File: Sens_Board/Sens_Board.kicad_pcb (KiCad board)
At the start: 4 copper layers, 87 x 84 mm, 170 parts, among them J1 Conn_01x09_Pin, J2 Conn_01x09_Pin, U1 74HC595, U10 74HC165, U11 74HC165, U12 74HC165, U13 74HC165, U14 74HC165, U15 74HC165, U2 74HC595, U3 74HC595, U4 74HC165, U5 74HC165, U6 74HC165, U7 74HC165, U8 74HC165, U9 74HC165

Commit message: fixes and optmierung
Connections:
- J3 pad A1: /RJ45/SchieberegisterInput/D7 -> /RJ45/SchieberegisterInput/D4
- J3 pad A2: /RJ45/SchieberegisterInput/D6 -> /RJ45/SchieberegisterInput/D5
- J3 pad A3: /RJ45/SchieberegisterInput/D5 -> /RJ45/SchieberegisterInput/D6
- J3 pad A4: /RJ45/SchieberegisterInput/D4 -> /RJ45/SchieberegisterInput/D7
- J3 pad A5: /RJ45/SchieberegisterInput/D3 -> /RJ45/SchieberegisterInput/D0
- J3 pad A6: /RJ45/SchieberegisterInput/D2 -> /RJ45/SchieberegisterInput/D1
- J3 pad A7: /RJ45/SchieberegisterInput/D1 -> /RJ45/SchieberegisterInput/D2
- J3 pad A8: /RJ45/SchieberegisterInput/D0 -> /RJ45/SchieberegisterInput/D3
- J3 pad B1: /RJ45/SchieberegisterInput1/D7 -> /RJ45/SchieberegisterInput1/D4
- J3 pad B2: /RJ45/SchieberegisterInput1/D6 -> /RJ45/SchieberegisterInput1/D5
- J3 pad B3: /RJ45/SchieberegisterInput1/D5 -> /RJ45/SchieberegisterInput1/D6
- J3 pad B4: /RJ45/SchieberegisterInput1/D4 -> /RJ45/SchieberegisterInput1/D7
- J3 pad B5: /RJ45/SchieberegisterInput1/D3 -> /RJ45/SchieberegisterInput1/D0
- J3 pad B6: /RJ45/SchieberegisterInput1/D2 -> /RJ45/SchieberegisterInput1/D1
- J3 pad B7: /RJ45/SchieberegisterInput1/D1 -> /RJ45/SchieberegisterInput1/D2
- J3 pad B8: /RJ45/SchieberegisterInput1/D0 -> /RJ45/SchieberegisterInput1/D3
- J3 pad C1: /RJ45/SchieberegisterInput2/D7 -> /RJ45/SchieberegisterInput2/D4
- J3 pad C2: /RJ45/SchieberegisterInput2/D6 -> /RJ45/SchieberegisterInput2/D5
- J3 pad C3: /RJ45/SchieberegisterInput2/D5 -> /RJ45/SchieberegisterInput2/D6
- J3 pad C4: /RJ45/SchieberegisterInput2/D4 -> /RJ45/SchieberegisterInput2/D7
- J3 pad C5: /RJ45/SchieberegisterInput2/D3 -> /RJ45/SchieberegisterInput2/D0
- J3 pad C6: /RJ45/SchieberegisterInput2/D2 -> /RJ45/SchieberegisterInput2/D1
- J3 pad C7: /RJ45/SchieberegisterInput2/D1 -> /RJ45/SchieberegisterInput2/D2
- J3 pad C8: /RJ45/SchieberegisterInput2/D0 -> /RJ45/SchieberegisterInput2/D3
- J3 pad D1: /RJ45/SchieberegisterInput3/D7 -> /RJ45/SchieberegisterInput3/D4
- J3 pad D2: /RJ45/SchieberegisterInput3/D6 -> /RJ45/SchieberegisterInput3/D5
- J3 pad D3: /RJ45/SchieberegisterInput3/D5 -> /RJ45/SchieberegisterInput3/D6
- J3 pad D4: /RJ45/SchieberegisterInput3/D4 -> /RJ45/SchieberegisterInput3/D7
- J3 pad D5: /RJ45/SchieberegisterInput3/D3 -> /RJ45/SchieberegisterInput3/D0
- J3 pad D6: /RJ45/SchieberegisterInput3/D2 -> /RJ45/SchieberegisterInput3/D1
- J3 pad D7: /RJ45/SchieberegisterInput3/D1 -> /RJ45/SchieberegisterInput3/D2
- J3 pad D8: /RJ45/SchieberegisterInput3/D0 -> /RJ45/SchieberegisterInput3/D3
- J3 pad E1: /RJ45/SchieberegisterInput4/D7 -> /RJ45/SchieberegisterInput4/D4
- J3 pad E2: /RJ45/SchieberegisterInput4/D6 -> /RJ45/SchieberegisterInput4/D5
- J3 pad E3: /RJ45/SchieberegisterInput4/D5 -> /RJ45/SchieberegisterInput4/D6
- J3 pad E4: /RJ45/SchieberegisterInput4/D4 -> /RJ45/SchieberegisterInput4/D7
- J3 pad E5: /RJ45/SchieberegisterInput4/D3 -> /RJ45/SchieberegisterInput4/D0
- J3 pad E6: /RJ45/SchieberegisterInput4/D2 -> /RJ45/SchieberegisterInput4/D1
- J3 pad E7: /RJ45/SchieberegisterInput4/D1 -> /RJ45/SchieberegisterInput4/D2
- J3 pad E8: /RJ45/SchieberegisterInput4/D0 -> /RJ45/SchieberegisterInput4/D3
- J3 pad F1: /RJ45/SchieberegisterInput5/D7 -> /RJ45/SchieberegisterInput5/D4
- J3 pad F11: (no net) -> GND
- J3 pad F12: GND -> /OutputShift1/Out3
- J3 pad F2: /RJ45/SchieberegisterInput5/D6 -> /RJ45/SchieberegisterInput5/D5
- J3 pad F3: /RJ45/SchieberegisterInput5/D5 -> /RJ45/SchieberegisterInput5/D6
- J3 pad F4: /RJ45/SchieberegisterInput5/D4 -> /RJ45/SchieberegisterInput5/D7
- J3 pad F5: /RJ45/SchieberegisterInput5/D3 -> /RJ45/SchieberegisterInput5/D0
- J3 pad F6: /RJ45/SchieberegisterInput5/D2 -> /RJ45/SchieberegisterInput5/D1
- J3 pad F7: /RJ45/SchieberegisterInput5/D1 -> /RJ45/SchieberegisterInput5/D2
- J3 pad F8: /RJ45/SchieberegisterInput5/D0 -> /RJ45/SchieberegisterInput5/D3
- J3 pad G1: /RJ45/SchieberegisterInput6/D7 -> /RJ45/SchieberegisterInput6/D4
- J3 pad G2: /RJ45/SchieberegisterInput6/D6 -> /RJ45/SchieberegisterInput6/D5
- J3 pad G3: /RJ45/SchieberegisterInput6/D5 -> /RJ45/SchieberegisterInput6/D6
- J3 pad G4: /RJ45/SchieberegisterInput6/D4 -> /RJ45/SchieberegisterInput6/D7
- J3 pad G5: /RJ45/SchieberegisterInput6/D3 -> /RJ45/SchieberegisterInput6/D0
- J3 pad G6: /RJ45/SchieberegisterInput6/D2 -> /RJ45/SchieberegisterInput6/D1
- J3 pad G7: /RJ45/SchieberegisterInput6/D1 -> /RJ45/SchieberegisterInput6/D2
- J3 pad G8: /RJ45/SchieberegisterInput6/D0 -> /RJ45/SchieberegisterInput6/D3
- J3 pad H1: /RJ45/SchieberegisterInput7/D7 -> /RJ45/SchieberegisterInput7/D4
- J3 pad H2: /RJ45/SchieberegisterInput7/D6 -> /RJ45/SchieberegisterInput7/D5
- J3 pad H3: /RJ45/SchieberegisterInput7/D5 -> /RJ45/SchieberegisterInput7/D6
- J3 pad H4: /RJ45/SchieberegisterInput7/D4 -> /RJ45/SchieberegisterInput7/D7
- J3 pad H5: /RJ45/SchieberegisterInput7/D3 -> /RJ45/SchieberegisterInput7/D0
- J3 pad H6: /RJ45/SchieberegisterInput7/D2 -> /RJ45/SchieberegisterInput7/D1
- J3 pad H7: /RJ45/SchieberegisterInput7/D1 -> /RJ45/SchieberegisterInput7/D2
- J3 pad H8: /RJ45/SchieberegisterInput7/D0 -> /RJ45/SchieberegisterInput7/D3
- J3 pad I1: /RJ45/SchieberegisterInput8/D7 -> /RJ45/SchieberegisterInput8/D4
- J3 pad I2: /RJ45/SchieberegisterInput8/D6 -> /RJ45/SchieberegisterInput8/D5
- J3 pad I3: /RJ45/SchieberegisterInput8/D5 -> /RJ45/SchieberegisterInput8/D6
- J3 pad I4: /RJ45/SchieberegisterInput8/D4 -> /RJ45/SchieberegisterInput8/D7
- J3 pad I5: /RJ45/SchieberegisterInput8/D3 -> /RJ45/SchieberegisterInput8/D0
- J3 pad I6: /RJ45/SchieberegisterInput8/D2 -> /RJ45/SchieberegisterInput8/D1
- J3 pad I7: /RJ45/SchieberegisterInput8/D1 -> /RJ45/SchieberegisterInput8/D2
- J3 pad I8: /RJ45/SchieberegisterInput8/D0 -> /RJ45/SchieberegisterInput8/D3
- J3 pad J1: /RJ45/SchieberegisterInput9/D7 -> /RJ45/SchieberegisterInput9/D4
- J3 pad J2: /RJ45/SchieberegisterInput9/D6 -> /RJ45/SchieberegisterInput9/D5
- J3 pad J3: /RJ45/SchieberegisterInput9/D5 -> /RJ45/SchieberegisterInput9/D6
- J3 pad J4: /RJ45/SchieberegisterInput9/D4 -> /RJ45/SchieberegisterInput9/D7
- J3 pad J5: /RJ45/SchieberegisterInput9/D3 -> /RJ45/SchieberegisterInput9/D0
- J3 pad J6: /RJ45/SchieberegisterInput9/D2 -> /RJ45/SchieberegisterInput9/D1
- J3 pad J7: /RJ45/SchieberegisterInput9/D1 -> /RJ45/SchieberegisterInput9/D2
- J3 pad J8: /RJ45/SchieberegisterInput9/D0 -> /RJ45/SchieberegisterInput9/D3
- J3 pad K1: /RJ45/SchieberegisterInput10/D7 -> /RJ45/SchieberegisterInput10/D4
- J3 pad K2: /RJ45/SchieberegisterInput10/D6 -> /RJ45/SchieberegisterInput10/D5
- J3 pad K3: /RJ45/SchieberegisterInput10/D5 -> /RJ45/SchieberegisterInput10/D6
- J3 pad K4: /RJ45/SchieberegisterInput10/D4 -> /RJ45/SchieberegisterInput10/D7
- J3 pad K5: /RJ45/SchieberegisterInput10/D3 -> /RJ45/SchieberegisterInput10/D0
- J3 pad K6: /RJ45/SchieberegisterInput10/D2 -> /RJ45/SchieberegisterInput10/D1
- J3 pad K7: /RJ45/SchieberegisterInput10/D1 -> /RJ45/SchieberegisterInput10/D2
- J3 pad K8: /RJ45/SchieberegisterInput10/D0 -> /RJ45/SchieberegisterInput10/D3
- J3 pad L1: /RJ45/SchieberegisterInput11/D7 -> /RJ45/SchieberegisterInput11/D4
- J3 pad L2: /RJ45/SchieberegisterInput11/D6 -> /RJ45/SchieberegisterInput11/D5
- J3 pad L3: /RJ45/SchieberegisterInput11/D5 -> /RJ45/SchieberegisterInput11/D6
- J3 pad L4: /RJ45/SchieberegisterInput11/D4 -> /RJ45/SchieberegisterInput11/D7
- J3 pad L5: /RJ45/SchieberegisterInput11/D3 -> /RJ45/SchieberegisterInput11/D0
- J3 pad L6: /RJ45/SchieberegisterInput11/D2 -> /RJ45/SchieberegisterInput11/D1
- J3 pad L7: /RJ45/SchieberegisterInput11/D1 -> /RJ45/SchieberegisterInput11/D2
- J3 pad L8: /RJ45/SchieberegisterInput11/D0 -> /RJ45/SchieberegisterInput11/D3
- R100 pad 2: /RJ45/SchieberegisterInput9/D7 -> /RJ45/SchieberegisterInput9/D4
- R101 pad 2: /RJ45/SchieberegisterInput9/D0 -> /RJ45/SchieberegisterInput9/D3
- R102 pad 2: /RJ45/SchieberegisterInput9/D1 -> /RJ45/SchieberegisterInput9/D2
- R103 pad 2: /RJ45/SchieberegisterInput9/D2 -> /RJ45/SchieberegisterInput9/D1
- R104 pad 2: /RJ45/SchieberegisterInput9/D3 -> /RJ45/SchieberegisterInput9/D0
- R105 pad 2: /RJ45/SchieberegisterInput10/D4 -> /RJ45/SchieberegisterInput10/D7
- R106 pad 2: /RJ45/SchieberegisterInput10/D5 -> /RJ45/SchieberegisterInput10/D6
- R107 pad 2: /RJ45/SchieberegisterInput10/D6 -> /RJ45/SchieberegisterInput10/D5
- R108 pad 2: /RJ45/SchieberegisterInput10/D7 -> /RJ45/SchieberegisterInput10/D4
- R109 pad 2: /RJ45/SchieberegisterInput10/D0 -> /RJ45/SchieberegisterInput10/D3
- R110 pad 2: /RJ45/SchieberegisterInput10/D1 -> /RJ45/SchieberegisterInput10/D2
- R111 pad 2: /RJ45/SchieberegisterInput10/D2 -> /RJ45/SchieberegisterInput10/D1
- R112 pad 2: /RJ45/SchieberegisterInput10/D3 -> /RJ45/SchieberegisterInput10/D0
- R113 pad 2: /RJ45/SchieberegisterInput11/D4 -> /RJ45/SchieberegisterInput11/D7
- R114 pad 2: /RJ45/SchieberegisterInput11/D5 -> /RJ45/SchieberegisterInput11/D6
- R115 pad 2: /RJ45/SchieberegisterInput11/D6 -> /RJ45/SchieberegisterInput11/D5
- R116 pad 2: /RJ45/SchieberegisterInput11/D7 -> /RJ45/SchieberegisterInput11/D4
- R117 pad 2: /RJ45/SchieberegisterInput11/D0 -> /RJ45/SchieberegisterInput11/D3
- R118 pad 2: /RJ45/SchieberegisterInput11/D1 -> /RJ45/SchieberegisterInput11/D2
- R119 pad 2: /RJ45/SchieberegisterInput11/D2 -> /RJ45/SchieberegisterInput11/D1
- R120 pad 2: /RJ45/SchieberegisterInput11/D3 -> /RJ45/SchieberegisterInput11/D0
- R25 pad 2: /RJ45/SchieberegisterInput/D4 -> /RJ45/SchieberegisterInput/D7
- R26 pad 2: /RJ45/SchieberegisterInput/D5 -> /RJ45/SchieberegisterInput/D6
- R27 pad 2: /RJ45/SchieberegisterInput/D6 -> /RJ45/SchieberegisterInput/D5
- R28 pad 2: /RJ45/SchieberegisterInput/D7 -> /RJ45/SchieberegisterInput/D4
- R29 pad 2: /RJ45/SchieberegisterInput/D0 -> /RJ45/SchieberegisterInput/D3
- R30 pad 2: /RJ45/SchieberegisterInput/D1 -> /RJ45/SchieberegisterInput/D2
- R31 pad 2: /RJ45/SchieberegisterInput/D2 -> /RJ45/SchieberegisterInput/D1
- R32 pad 2: /RJ45/SchieberegisterInput/D3 -> /RJ45/SchieberegisterInput/D0
- R33 pad 2: /RJ45/SchieberegisterInput2/D4 -> /RJ45/SchieberegisterInput2/D7
- R34 pad 2: /RJ45/SchieberegisterInput2/D5 -> /RJ45/SchieberegisterInput2/D6
- R35 pad 2: /RJ45/SchieberegisterInput2/D6 -> /RJ45/SchieberegisterInput2/D5
- R36 pad 2: /RJ45/SchieberegisterInput2/D7 -> /RJ45/SchieberegisterInput2/D4
- R37 pad 2: /RJ45/SchieberegisterInput2/D0 -> /RJ45/SchieberegisterInput2/D3
- R38 pad 2: /RJ45/SchieberegisterInput2/D1 -> /RJ45/SchieberegisterInput2/D2
- R39 pad 2: /RJ45/SchieberegisterInput2/D2 -> /RJ45/SchieberegisterInput2/D1
- R40 pad 2: /RJ45/SchieberegisterInput2/D3 -> /RJ45/SchieberegisterInput2/D0
- R41 pad 2: /RJ45/SchieberegisterInput1/D4 -> /RJ45/SchieberegisterInput1/D7
- R42 pad 2: /RJ45/SchieberegisterInput1/D5 -> /RJ45/SchieberegisterInput1/D6
- R43 pad 2: /RJ45/SchieberegisterInput1/D6 -> /RJ45/SchieberegisterInput1/D5
- R44 pad 2: /RJ45/SchieberegisterInput1/D7 -> /RJ45/SchieberegisterInput1/D4
- R45 pad 2: /RJ45/SchieberegisterInput1/D0 -> /RJ45/SchieberegisterInput1/D3
- R46 pad 2: /RJ45/SchieberegisterInput1/D1 -> /RJ45/SchieberegisterInput1/D2
- R47 pad 2: /RJ45/SchieberegisterInput1/D2 -> /RJ45/SchieberegisterInput1/D1
- R48 pad 2: /RJ45/SchieberegisterInput1/D3 -> /RJ45/SchieberegisterInput1/D0
- R49 pad 2: /RJ45/SchieberegisterInput3/D4 -> /RJ45/SchieberegisterInput3/D7
- R50 pad 2: /RJ45/SchieberegisterInput3/D5 -> /RJ45/SchieberegisterInput3/D6
- R51 pad 2: /RJ45/SchieberegisterInput3/D6 -> /RJ45/SchieberegisterInput3/D5
- R52 pad 2: /RJ45/SchieberegisterInput3/D7 -> /RJ45/SchieberegisterInput3/D4
- R53 pad 2: /RJ45/SchieberegisterInput3/D0 -> /RJ45/SchieberegisterInput3/D3
- R54 pad 2: /RJ45/SchieberegisterInput3/D1 -> /RJ45/SchieberegisterInput3/D2
- R55 pad 2: /RJ45/SchieberegisterInput3/D2 -> /RJ45/SchieberegisterInput3/D1
- R56 pad 2: /RJ45/SchieberegisterInput3/D3 -> /RJ45/SchieberegisterInput3/D0
- R57 pad 2: /RJ45/SchieberegisterInput4/D4 -> /RJ45/SchieberegisterInput4/D7
- R58 pad 2: /RJ45/SchieberegisterInput4/D5 -> /RJ45/SchieberegisterInput4/D6
- R59 pad 2: /RJ45/SchieberegisterInput4/D6 -> /RJ45/SchieberegisterInput4/D5
- R60 pad 2: /RJ45/SchieberegisterInput4/D7 -> /RJ45/SchieberegisterInput4/D4
- R61 pad 2: /RJ45/SchieberegisterInput4/D0 -> /RJ45/SchieberegisterInput4/D3
- R62 pad 2: /RJ45/SchieberegisterInput4/D1 -> /RJ45/SchieberegisterInput4/D2
- R63 pad 2: /RJ45/SchieberegisterInput4/D2 -> /RJ45/SchieberegisterInput4/D1
- R64 pad 2: /RJ45/SchieberegisterInput4/D3 -> /RJ45/SchieberegisterInput4/D0
- R65 pad 2: /RJ45/SchieberegisterInput5/D4 -> /RJ45/SchieberegisterInput5/D7
- R66 pad 2: /RJ45/SchieberegisterInput5/D5 -> /RJ45/SchieberegisterInput5/D6
- R67 pad 2: /RJ45/SchieberegisterInput5/D6 -> /RJ45/SchieberegisterInput5/D5
- R68 pad 2: /RJ45/SchieberegisterInput5/D7 -> /RJ45/SchieberegisterInput5/D4
- R69 pad 2: /RJ45/SchieberegisterInput5/D0 -> /RJ45/SchieberegisterInput5/D3
- R70 pad 2: /RJ45/SchieberegisterInput5/D1 -> /RJ45/SchieberegisterInput5/D2
- R71 pad 2: /RJ45/SchieberegisterInput5/D2 -> /RJ45/SchieberegisterInput5/D1
- R72 pad 2: /RJ45/SchieberegisterInput5/D3 -> /RJ45/SchieberegisterInput5/D0
- R73 pad 2: /RJ45/SchieberegisterInput6/D4 -> /RJ45/SchieberegisterInput6/D7
- R74 pad 2: /RJ45/SchieberegisterInput6/D5 -> /RJ45/SchieberegisterInput6/D6
- R75 pad 2: /RJ45/SchieberegisterInput6/D6 -> /RJ45/SchieberegisterInput6/D5
- R76 pad 2: /RJ45/SchieberegisterInput6/D7 -> /RJ45/SchieberegisterInput6/D4
- R77 pad 2: /RJ45/SchieberegisterInput6/D0 -> /RJ45/SchieberegisterInput6/D3
- R78 pad 2: /RJ45/SchieberegisterInput6/D1 -> /RJ45/SchieberegisterInput6/D2
- R79 pad 2: /RJ45/SchieberegisterInput6/D2 -> /RJ45/SchieberegisterInput6/D1
- R80 pad 2: /RJ45/SchieberegisterInput6/D3 -> /RJ45/SchieberegisterInput6/D0
- R81 pad 2: /RJ45/SchieberegisterInput7/D4 -> /RJ45/SchieberegisterInput7/D7
- R82 pad 2: /RJ45/SchieberegisterInput7/D5 -> /RJ45/SchieberegisterInput7/D6
- R83 pad 2: /RJ45/SchieberegisterInput7/D6 -> /RJ45/SchieberegisterInput7/D5
- R84 pad 2: /RJ45/SchieberegisterInput7/D7 -> /RJ45/SchieberegisterInput7/D4
- R85 pad 2: /RJ45/SchieberegisterInput7/D0 -> /RJ45/SchieberegisterInput7/D3
- R86 pad 2: /RJ45/SchieberegisterInput7/D1 -> /RJ45/SchieberegisterInput7/D2
- R87 pad 2: /RJ45/SchieberegisterInput7/D2 -> /RJ45/SchieberegisterInput7/D1
- R88 pad 2: /RJ45/SchieberegisterInput7/D3 -> /RJ45/SchieberegisterInput7/D0
- R89 pad 2: /RJ45/SchieberegisterInput8/D4 -> /RJ45/SchieberegisterInput8/D7
- R90 pad 2: /RJ45/SchieberegisterInput8/D5 -> /RJ45/SchieberegisterInput8/D6
- R91 pad 2: /RJ45/SchieberegisterInput8/D6 -> /RJ45/SchieberegisterInput8/D5
- R92 pad 2: /RJ45/SchieberegisterInput8/D7 -> /RJ45/SchieberegisterInput8/D4
- R93 pad 2: /RJ45/SchieberegisterInput8/D0 -> /RJ45/SchieberegisterInput8/D3
- R94 pad 2: /RJ45/SchieberegisterInput8/D1 -> /RJ45/SchieberegisterInput8/D2
- R95 pad 2: /RJ45/SchieberegisterInput8/D2 -> /RJ45/SchieberegisterInput8/D1
- R96 pad 2: /RJ45/SchieberegisterInput8/D3 -> /RJ45/SchieberegisterInput8/D0
- R97 pad 2: /RJ45/SchieberegisterInput9/D4 -> /RJ45/SchieberegisterInput9/D7
- R98 pad 2: /RJ45/SchieberegisterInput9/D5 -> /RJ45/SchieberegisterInput9/D6
- R99 pad 2: /RJ45/SchieberegisterInput9/D6 -> /RJ45/SchieberegisterInput9/D5
- U10 pad 11: /RJ45/SchieberegisterInput6/D3 -> /RJ45/SchieberegisterInput6/D0
- U10 pad 12: /RJ45/SchieberegisterInput6/D2 -> /RJ45/SchieberegisterInput6/D1
- U10 pad 13: /RJ45/SchieberegisterInput6/D1 -> /RJ45/SchieberegisterInput6/D2
- U10 pad 14: /RJ45/SchieberegisterInput6/D0 -> /RJ45/SchieberegisterInput6/D3
- U10 pad 3: /RJ45/SchieberegisterInput6/D7 -> /RJ45/SchieberegisterInput6/D4
- U10 pad 4: /RJ45/SchieberegisterInput6/D6 -> /RJ45/SchieberegisterInput6/D5
- U10 pad 5: /RJ45/SchieberegisterInput6/D5 -> /RJ45/SchieberegisterInput6/D6
- U10 pad 6: /RJ45/SchieberegisterInput6/D4 -> /RJ45/SchieberegisterInput6/D7
- U11 pad 11: /RJ45/SchieberegisterInput7/D3 -> /RJ45/SchieberegisterInput7/D0
- U11 pad 12: /RJ45/SchieberegisterInput7/D2 -> /RJ45/SchieberegisterInput7/D1
- U11 pad 13: /RJ45/SchieberegisterInput7/D1 -> /RJ45/SchieberegisterInput7/D2
- U11 pad 14: /RJ45/SchieberegisterInput7/D0 -> /RJ45/SchieberegisterInput7/D3
- U11 pad 3: /RJ45/SchieberegisterInput7/D7 -> /RJ45/SchieberegisterInput7/D4
- U11 pad 4: /RJ45/SchieberegisterInput7/D6 -> /RJ45/SchieberegisterInput7/D5
- U11 pad 5: /RJ45/SchieberegisterInput7/D5 -> /RJ45/SchieberegisterInput7/D6
- U11 pad 6: /RJ45/SchieberegisterInput7/D4 -> /RJ45/SchieberegisterInput7/D7
- U12 pad 11: /RJ45/SchieberegisterInput8/D3 -> /RJ45/SchieberegisterInput8/D0
- U12 pad 12: /RJ45/SchieberegisterInput8/D2 -> /RJ45/SchieberegisterInput8/D1
- U12 pad 13: /RJ45/SchieberegisterInput8/D1 -> /RJ45/SchieberegisterInput8/D2
- U12 pad 14: /RJ45/SchieberegisterInput8/D0 -> /RJ45/SchieberegisterInput8/D3
- U12 pad 3: /RJ45/SchieberegisterInput8/D7 -> /RJ45/SchieberegisterInput8/D4
- U12 pad 4: /RJ45/SchieberegisterInput8/D6 -> /RJ45/SchieberegisterInput8/D5
- U12 pad 5: /RJ45/SchieberegisterInput8/D5 -> /RJ45/SchieberegisterInput8/D6
- U12 pad 6: /RJ45/SchieberegisterInput8/D4 -> /RJ45/SchieberegisterInput8/D7
- U13 pad 11: /RJ45/SchieberegisterInput9/D3 -> /RJ45/SchieberegisterInput9/D0
- U13 pad 12: /RJ45/SchieberegisterInput9/D2 -> /RJ45/SchieberegisterInput9/D1
- U13 pad 13: /RJ45/SchieberegisterInput9/D1 -> /RJ45/SchieberegisterInput9/D2
- U13 pad 14: /RJ45/SchieberegisterInput9/D0 -> /RJ45/SchieberegisterInput9/D3
- U13 pad 3: /RJ45/SchieberegisterInput9/D7 -> /RJ45/SchieberegisterInput9/D4
- U13 pad 4: /RJ45/SchieberegisterInput9/D6 -> /RJ45/SchieberegisterInput9/D5
- U13 pad 5: /RJ45/SchieberegisterInput9/D5 -> /RJ45/SchieberegisterInput9/D6
- U13 pad 6: /RJ45/SchieberegisterInput9/D4 -> /RJ45/SchieberegisterInput9/D7
- U14 pad 11: /RJ45/SchieberegisterInput10/D3 -> /RJ45/SchieberegisterInput10/D0
- U14 pad 12: /RJ45/SchieberegisterInput10/D2 -> /RJ45/SchieberegisterInput10/D1
- U14 pad 13: /RJ45/SchieberegisterInput10/D1 -> /RJ45/SchieberegisterInput10/D2
- U14 pad 14: /RJ45/SchieberegisterInput10/D0 -> /RJ45/SchieberegisterInput10/D3
- U14 pad 3: /RJ45/SchieberegisterInput10/D7 -> /RJ45/SchieberegisterInput10/D4
- U14 pad 4: /RJ45/SchieberegisterInput10/D6 -> /RJ45/SchieberegisterInput10/D5
- U14 pad 5: /RJ45/SchieberegisterInput10/D5 -> /RJ45/SchieberegisterInput10/D6
- U14 pad 6: /RJ45/SchieberegisterInput10/D4 -> /RJ45/SchieberegisterInput10/D7
- U15 pad 11: /RJ45/SchieberegisterInput11/D3 -> /RJ45/SchieberegisterInput11/D0
- U15 pad 12: /RJ45/SchieberegisterInput11/D2 -> /RJ45/SchieberegisterInput11/D1
- U15 pad 13: /RJ45/SchieberegisterInput11/D1 -> /RJ45/SchieberegisterInput11/D2
- U15 pad 14: /RJ45/SchieberegisterInput11/D0 -> /RJ45/SchieberegisterInput11/D3
- U15 pad 3: /RJ45/SchieberegisterInput11/D7 -> /RJ45/SchieberegisterInput11/D4
- U15 pad 4: /RJ45/SchieberegisterInput11/D6 -> /RJ45/SchieberegisterInput11/D5
- U15 pad 5: /RJ45/SchieberegisterInput11/D5 -> /RJ45/SchieberegisterInput11/D6
- U15 pad 6: /RJ45/SchieberegisterInput11/D4 -> /RJ45/SchieberegisterInput11/D7
- U4 pad 11: /RJ45/SchieberegisterInput/D3 -> /RJ45/SchieberegisterInput/D0
- U4 pad 12: /RJ45/SchieberegisterInput/D2 -> /RJ45/SchieberegisterInput/D1
- U4 pad 13: /RJ45/SchieberegisterInput/D1 -> /RJ45/SchieberegisterInput/D2
- U4 pad 14: /RJ45/SchieberegisterInput/D0 -> /RJ45/SchieberegisterInput/D3
- U4 pad 3: /RJ45/SchieberegisterInput/D7 -> /RJ45/SchieberegisterInput/D4
- U4 pad 4: /RJ45/SchieberegisterInput/D6 -> /RJ45/SchieberegisterInput/D5
- U4 pad 5: /RJ45/SchieberegisterInput/D5 -> /RJ45/SchieberegisterInput/D6
- U4 pad 6: /RJ45/SchieberegisterInput/D4 -> /RJ45/SchieberegisterInput/D7
- U5 pad 11: /RJ45/SchieberegisterInput1/D3 -> /RJ45/SchieberegisterInput1/D0
- U5 pad 12: /RJ45/SchieberegisterInput1/D2 -> /RJ45/SchieberegisterInput1/D1
- U5 pad 13: /RJ45/SchieberegisterInput1/D1 -> /RJ45/SchieberegisterInput1/D2
- U5 pad 14: /RJ45/SchieberegisterInput1/D0 -> /RJ45/SchieberegisterInput1/D3
- U5 pad 3: /RJ45/SchieberegisterInput1/D7 -> /RJ45/SchieberegisterInput1/D4
- U5 pad 4: /RJ45/SchieberegisterInput1/D6 -> /RJ45/SchieberegisterInput1/D5
- U5 pad 5: /RJ45/SchieberegisterInput1/D5 -> /RJ45/SchieberegisterInput1/D6
- U5 pad 6: /RJ45/SchieberegisterInput1/D4 -> /RJ45/SchieberegisterInput1/D7
- U6 pad 11: /RJ45/SchieberegisterInput2/D3 -> /RJ45/SchieberegisterInput2/D0
- U6 pad 12: /RJ45/SchieberegisterInput2/D2 -> /RJ45/SchieberegisterInput2/D1
- U6 pad 13: /RJ45/SchieberegisterInput2/D1 -> /RJ45/SchieberegisterInput2/D2
- U6 pad 14: /RJ45/SchieberegisterInput2/D0 -> /RJ45/SchieberegisterInput2/D3
- U6 pad 3: /RJ45/SchieberegisterInput2/D7 -> /RJ45/SchieberegisterInput2/D4
- U6 pad 4: /RJ45/SchieberegisterInput2/D6 -> /RJ45/SchieberegisterInput2/D5
- U6 pad 5: /RJ45/SchieberegisterInput2/D5 -> /RJ45/SchieberegisterInput2/D6
- U6 pad 6: /RJ45/SchieberegisterInput2/D4 -> /RJ45/SchieberegisterInput2/D7
- U7 pad 11: /RJ45/SchieberegisterInput3/D3 -> /RJ45/SchieberegisterInput3/D0
- U7 pad 12: /RJ45/SchieberegisterInput3/D2 -> /RJ45/SchieberegisterInput3/D1
- U7 pad 13: /RJ45/SchieberegisterInput3/D1 -> /RJ45/SchieberegisterInput3/D2
- U7 pad 14: /RJ45/SchieberegisterInput3/D0 -> /RJ45/SchieberegisterInput3/D3
- U7 pad 3: /RJ45/SchieberegisterInput3/D7 -> /RJ45/SchieberegisterInput3/D4
- U7 pad 4: /RJ45/SchieberegisterInput3/D6 -> /RJ45/SchieberegisterInput3/D5
- U7 pad 5: /RJ45/SchieberegisterInput3/D5 -> /RJ45/SchieberegisterInput3/D6
- U7 pad 6: /RJ45/SchieberegisterInput3/D4 -> /RJ45/SchieberegisterInput3/D7
- U8 pad 11: /RJ45/SchieberegisterInput4/D3 -> /RJ45/SchieberegisterInput4/D0
- U8 pad 12: /RJ45/SchieberegisterInput4/D2 -> /RJ45/SchieberegisterInput4/D1
- U8 pad 13: /RJ45/SchieberegisterInput4/D1 -> /RJ45/SchieberegisterInput4/D2
- U8 pad 14: /RJ45/SchieberegisterInput4/D0 -> /RJ45/SchieberegisterInput4/D3
- U8 pad 3: /RJ45/SchieberegisterInput4/D7 -> /RJ45/SchieberegisterInput4/D4
- U8 pad 4: /RJ45/SchieberegisterInput4/D6 -> /RJ45/SchieberegisterInput4/D5
- U8 pad 5: /RJ45/SchieberegisterInput4/D5 -> /RJ45/SchieberegisterInput4/D6
- U8 pad 6: /RJ45/SchieberegisterInput4/D4 -> /RJ45/SchieberegisterInput4/D7
- U9 pad 11: /RJ45/SchieberegisterInput5/D3 -> /RJ45/SchieberegisterInput5/D0
- U9 pad 12: /RJ45/SchieberegisterInput5/D2 -> /RJ45/SchieberegisterInput5/D1
- U9 pad 13: /RJ45/SchieberegisterInput5/D1 -> /RJ45/SchieberegisterInput5/D2
- U9 pad 14: /RJ45/SchieberegisterInput5/D0 -> /RJ45/SchieberegisterInput5/D3
- U9 pad 3: /RJ45/SchieberegisterInput5/D7 -> /RJ45/SchieberegisterInput5/D4
- U9 pad 4: /RJ45/SchieberegisterInput5/D6 -> /RJ45/SchieberegisterInput5/D5
- U9 pad 5: /RJ45/SchieberegisterInput5/D5 -> /RJ45/SchieberegisterInput5/D6
- U9 pad 6: /RJ45/SchieberegisterInput5/D4 -> /RJ45/SchieberegisterInput5/D7
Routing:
- net /OutputShift1/Out3: track 0.00 -> 69.2 mm, vias 0 -> 1
- net /RJ45/SchieberegisterInput1/D7: track 47.3 -> 40.7 mm
- net /RJ45/SchieberegisterInput1/D4: track 40.7 -> 47.3 mm
- net /RJ45/SchieberegisterInput3/D7: track 46.4 -> 40.3 mm
- net /RJ45/SchieberegisterInput3/D4: track 40.3 -> 46.4 mm
- net /RJ45/SchieberegisterInput4/D7: track 18.7 -> 24.7 mm
- net /RJ45/SchieberegisterInput4/D4: track 24.7 -> 18.7 mm
- net /RJ45/SchieberegisterInput6/D7: track 18.8 -> 24.8 mm
- net /RJ45/SchieberegisterInput6/D4: track 24.8 -> 18.8 mm
- net /RJ45/SchieberegisterInput11/D7: track 46.3 -> 40.4 mm
- net /RJ45/SchieberegisterInput11/D4: track 40.4 -> 46.3 mm
- net /RJ45/SchieberegisterInput2/D7: track 19.0 -> 24.8 mm
- net /RJ45/SchieberegisterInput2/D4: track 24.8 -> 19.0 mm
- net /RJ45/SchieberegisterInput8/D7: track 19.2 -> 25.0 mm
- net /RJ45/SchieberegisterInput8/D4: track 25.0 -> 19.2 mm
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
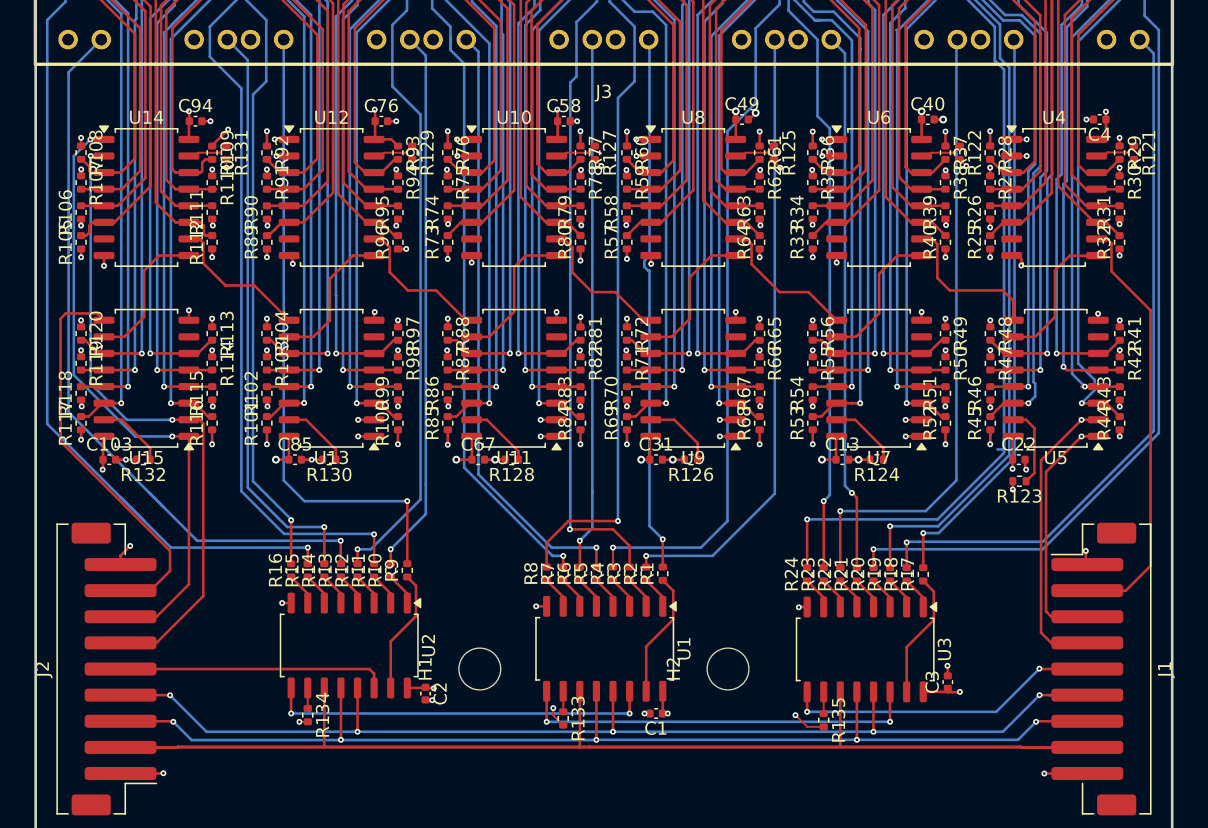
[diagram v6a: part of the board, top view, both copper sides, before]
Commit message: prettify silkscreen
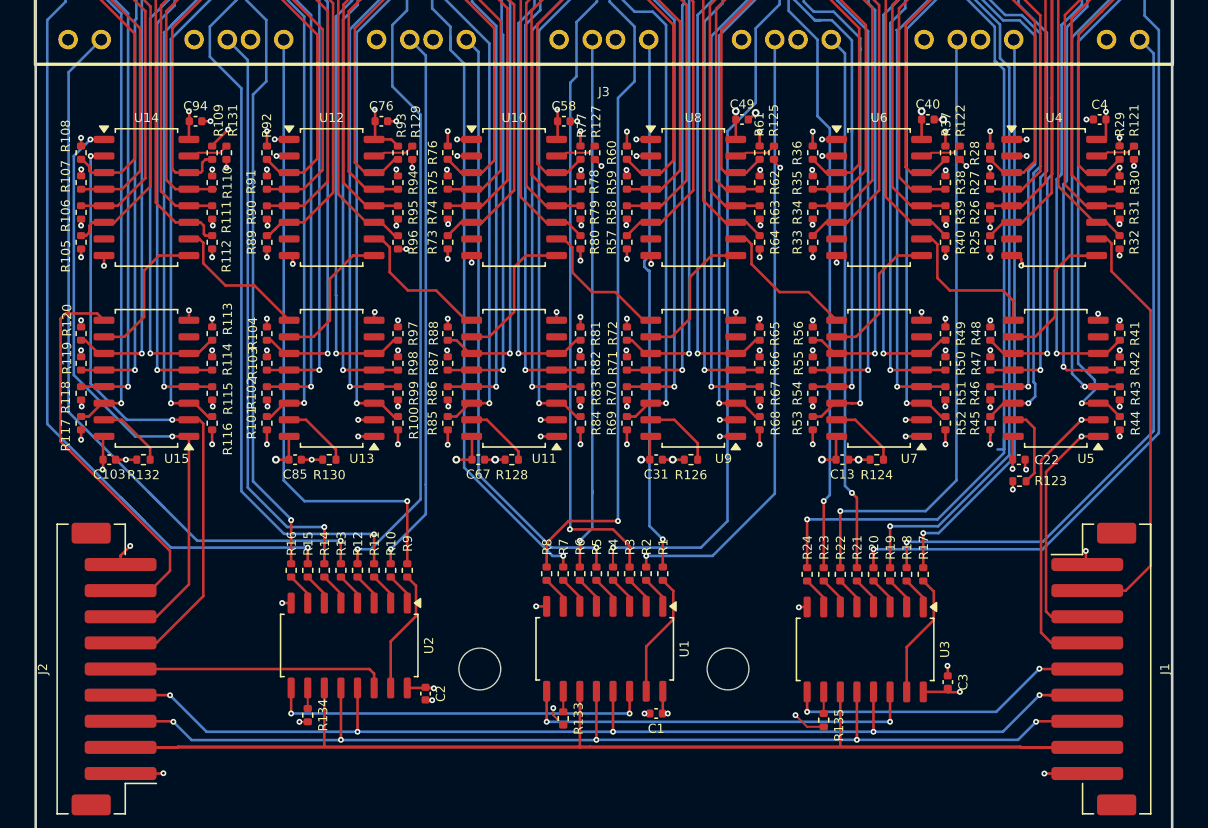
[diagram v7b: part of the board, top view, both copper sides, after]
